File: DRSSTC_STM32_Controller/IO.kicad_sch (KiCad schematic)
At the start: 32 parts, among them J1 Conn_01x04, J10 Screw_Terminal_01x02, J11 Screw_Terminal_01x02, J12 Screw_Terminal_01x02, J6 Screw_Terminal_01x02, J7 Screw_Terminal_01x02, Q10 2N7002, Q5 2N7002, Q6 2N7002, Q7 2N7002, Q8 2N7002, Q9 2N7002

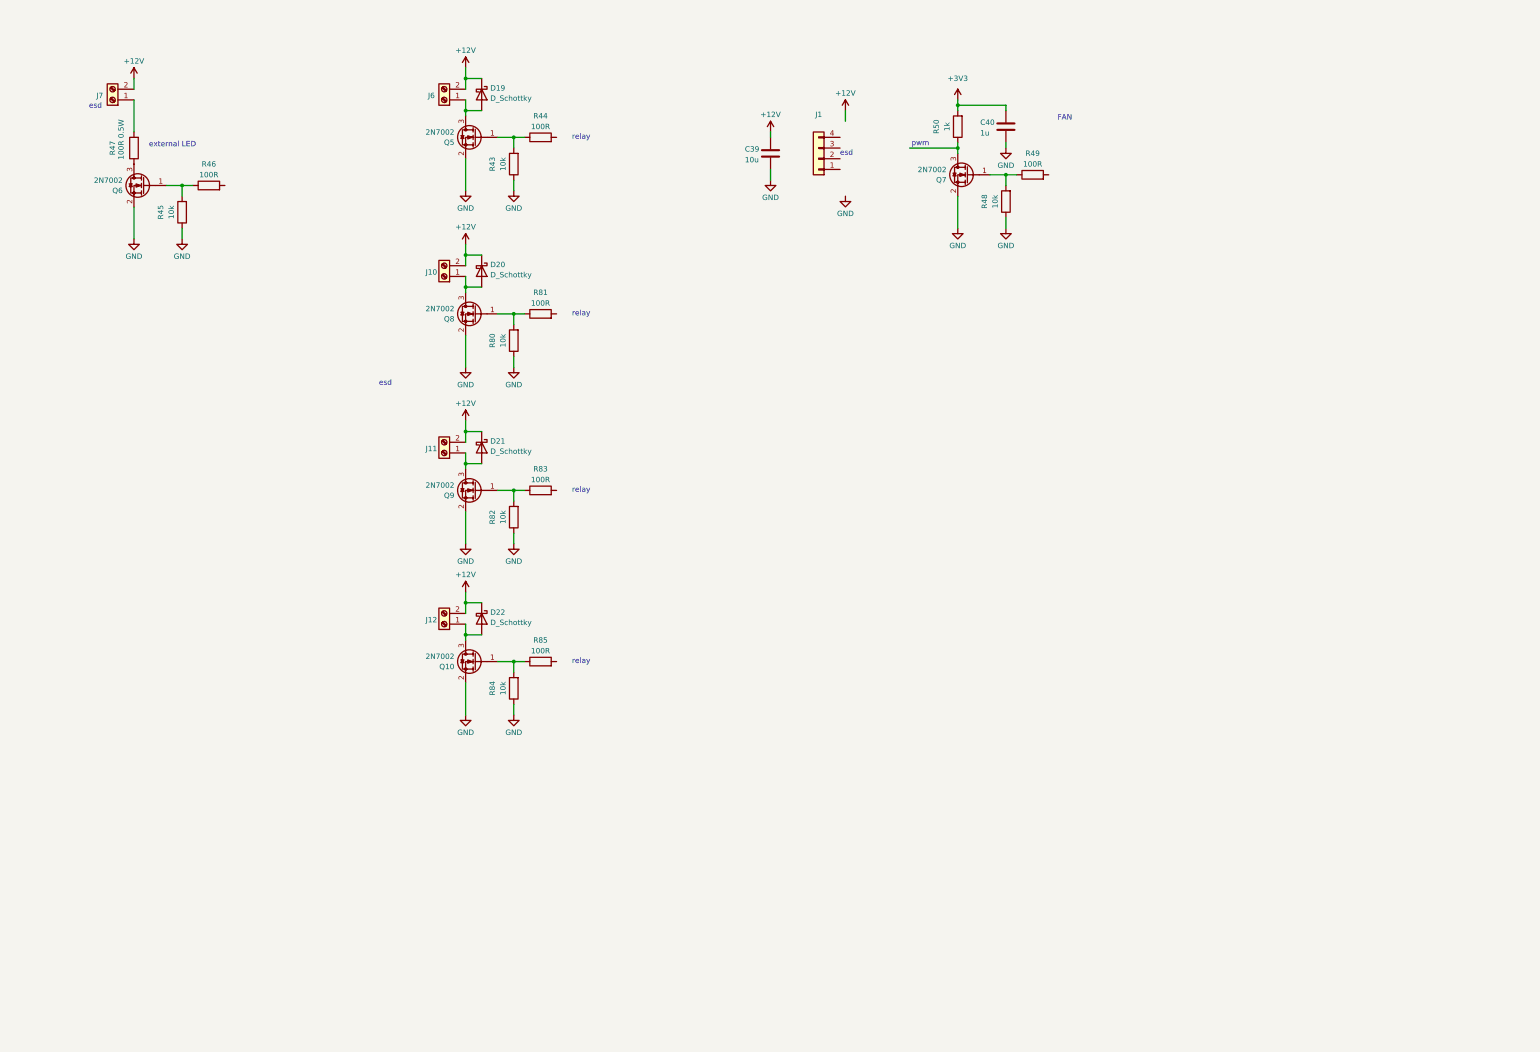
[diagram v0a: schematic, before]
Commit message: update the feedback stage simulation & controller schematic
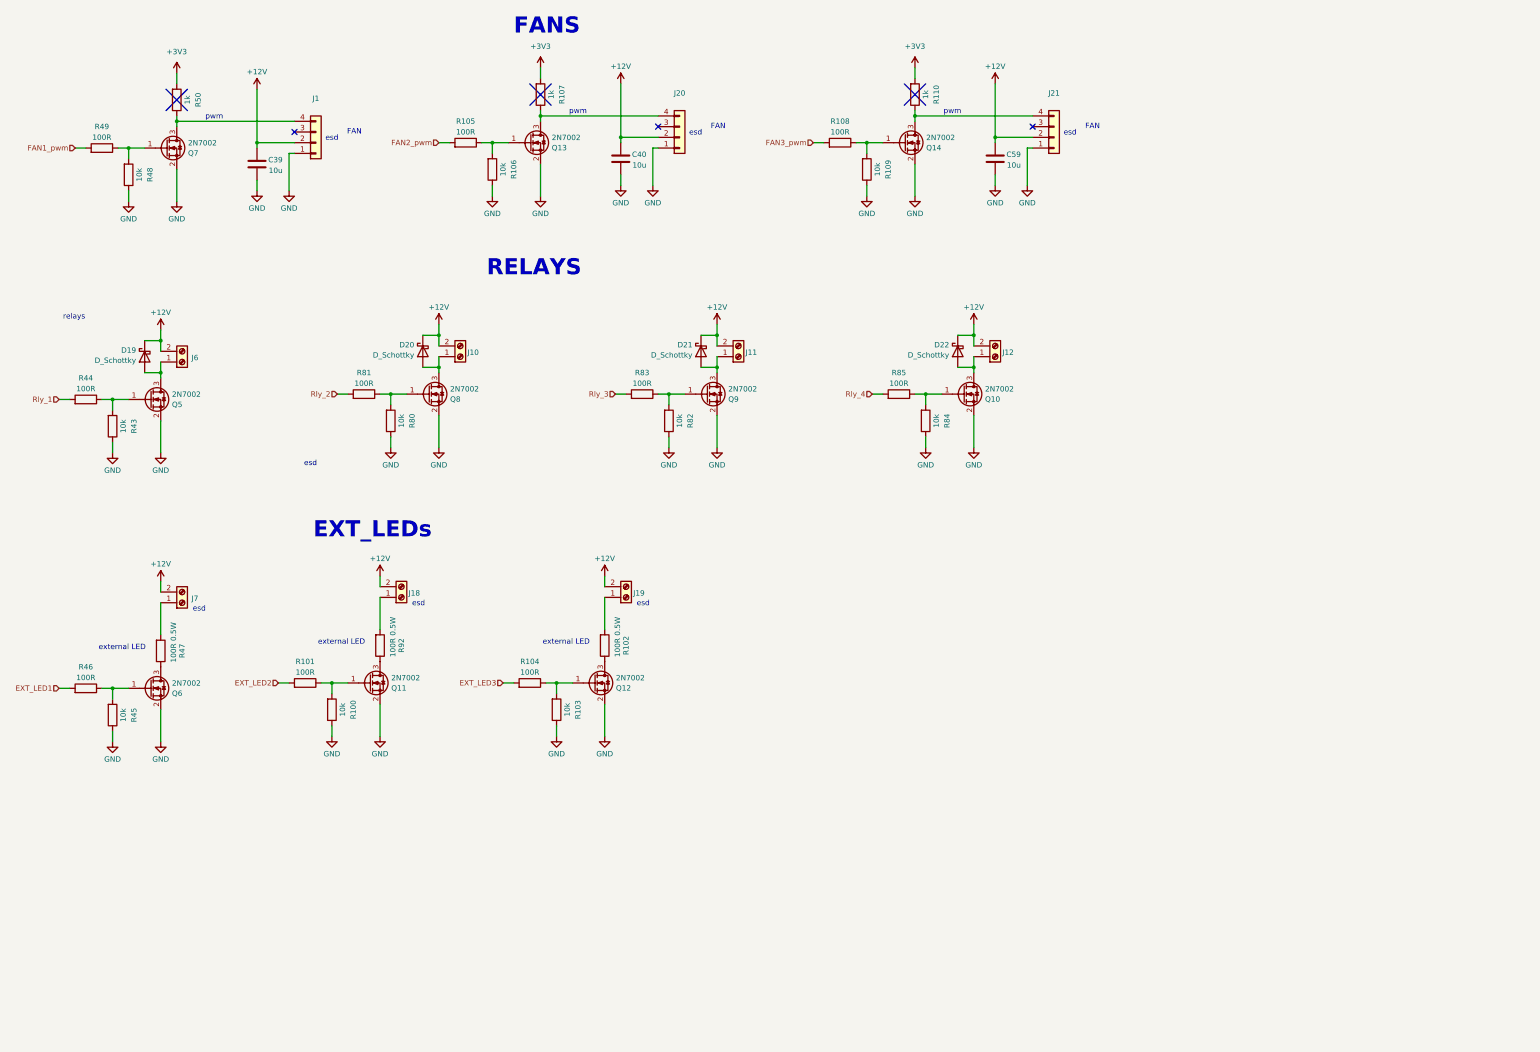
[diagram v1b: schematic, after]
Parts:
- added C59: 10u, Capacitor_SMD:C_0805_2012Metric, symbol Device:C
- added J18, J19: Screw_Terminal_01x02, TerminalBlock_Altech:Altech_AK100_1x02_P5.00mm, symbol Connector:Screw_Terminal_01x02
- added J20, J21: Conn_01x04, symbol Connector_Generic:Conn_01x04
- added Q11, Q12, Q13, Q14: 2N7002, Package_TO_SOT_SMD:SOT-23, symbol Transistor_FET:2N7002
- added R100, R103, R106, R109: 10k, Resistor_SMD:R_0805_2012Metric, symbol Device:R
- added R101, R104, R105, R108: 100R, Resistor_SMD:R_0805_2012Metric, symbol Device:R
- added R102, R92: 100R 0.5W, Resistor_SMD:R_0805_2012Metric, symbol Device:R
- added R107, R110: 1k, Resistor_SMD:R_0805_2012Metric, symbol Device:R
- C40: value 1u -> 10u
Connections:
- net +12V: now also C40.1, J1.2 (Pin_2), C59.1, J18.2 (Pin_2), J19.2 (Pin_2), J20.2 (Pin_2), J21.2 (Pin_2)
- net +3V3: now also R107.2, R110.2; no longer C40.1
- net GND: now also J1.1 (Pin_1), C59.2, J20.1 (Pin_1), J21.1 (Pin_1), Q11.2 (S), Q12.2 (S), Q13.2 (S), Q14.2 (S), R100.1, R103.1, R106.1, R109.1
- net Rly_3: now reaches R83.2
- net Rly_4: now reaches R85.2
- net FAN1_pwm: now reaches R49.2
- net Rly_2: now reaches R81.2
- net Rly_1: now reaches R44.2
- net EXT_LED1: now reaches R46.2
- net at Q7.3 (D), R50.1: now also J1.4 (Pin_4)
- new net: Q13.1 (G), R105.1, R106.2
- new net: Q14.1 (G), R108.1, R109.2
- new net: J21.4 (Pin_4), Q14.3 (D), R110.1
- new net: Q12.3 (D), R102.1
- new net: J19.1 (Pin_1), R102.2
- new net: Q11.1 (G), R100.2, R101.1
- new net: J18.1 (Pin_1), R92.2
- new net: Q12.1 (G), R103.2, R104.1
- new net: Q11.3 (D), R92.1
- new net: J20.4 (Pin_4), Q13.3 (D), R107.1
- new net EXT_LED2: R101.2
- new net EXT_LED3: R104.2
- new net FAN2_pwm: R105.2
- new net FAN3_pwm: R108.2
- no-connect marks 0 -> 3
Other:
- note added: "EXT_LEDs"
- note added: "FANS"
- note added: "RELAYS"
- note added: "relays"
- note removed: "relay"
- moved on the sheet: C39, D19, D20, D21, D22, J1, J10, J11, J12, J6, J7, Q10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

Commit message: update conroller schematics
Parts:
- removed J1, J20, J21: Conn_01x04, symbol Connector_Generic:Conn_01x04
- removed J10, J11, J12, J18, J19, J6, J7: Screw_Terminal_01x02, TerminalBlock_Altech:Altech_AK100_1x02_P5.00mm, symbol Connector:Screw_Terminal_01x02
- added C76: 10u, Capacitor_SMD:C_0805_2012Metric, symbol Device:C
- added Q19, Q20: 2N7002, Package_TO_SOT_SMD:SOT-23, symbol Transistor_FET:2N7002
- added R127, R130: 100R, Resistor_SMD:R_0805_2012Metric, symbol Device:R
- added R128, R131: 10k, Resistor_SMD:R_0805_2012Metric, symbol Device:R
- added R129: 1k, Resistor_SMD:R_0805_2012Metric, symbol Device:R
- added R132: 100R 0.5W, Resistor_SMD:R_0805_2012Metric, symbol Device:R
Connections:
- net +12V: now also C76.1
- net +3V3: now also R129.2
- net GND: now also C76.2, Q19.2 (S), Q20.2 (S), R128.1, R131.1
- net Relay4: now reaches D22.2 (A), Q10.3 (D)
- net FAN3cntrl: now reaches Q14.3 (D), R110.1
- net LED3: now reaches R102.2
- net Relay2: now reaches D20.2 (A), Q8.3 (D)
- net Relay3: now reaches D21.2 (A), Q9.3 (D)
- net LED1: now reaches R47.2
- net LED2: now reaches R92.2
- net FAN2cntrl: now reaches Q13.3 (D), R107.1
- net Relay1: now reaches D19.2 (A), Q5.3 (D)
- net FAN1cntrl: now reaches Q7.3 (D), R50.1
- new net: Q19.1 (G), R127.1, R128.2
- new net: Q20.1 (G), R130.1, R131.2
- new net: Q20.3 (D), R132.1
- new net EXT_LED4: R130.2
- new net FAN4_pwm: R127.2
- new net FAN4cntrl: Q19.3 (D), R129.1
- new net LED4: R132.2
- no-connect marks 3 -> 0
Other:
- note removed: "FAN"
- note removed: "relays"
- moved on the sheet: C39, C40, C59, D19, D20, D21, D22, Q10, Q11, Q12, Q13, Q14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

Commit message: assign footprints
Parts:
- D19, D20, D21, D22: footprint (none) -> Diode_SMD:D_SOD-128
- R100, R101, R103, R104, R105, R106, R107, R108, R109, R110, R127, R128, R129, R130, R131, R43, R44, R45, R46, R48, R49, R50, R80, R81, R82, R83, R84, R85: footprint Resistor_SMD:R_0805_2012Metric -> Resistor_SMD:R_0603_1608Metric
- R102, R132, R47, R92: footprint Resistor_SMD:R_0805_2012Metric -> Resistor_THT:R_Axial_DIN0309_L9.0mm_D3.2mm_P12.70mm_Horizontal
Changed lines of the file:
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@@
 			)
 		)
-		(property "Footprint" ""
+		(property "Footprint" "Diode_SMD:D_SOD-128"
 			(at 276.86 53.34 0)
 			(hide yes)
@@
 			)
 		)
-		(property "Footprint" "Resistor_SMD:R_0805_2012Metric"
+		(property "Footprint" "Resistor_SMD:R_0603_1608Metric"
 			(at 320.04 144.018 90)
 			(hide yes)
@@
 			)
 		)
-		(property "Footprint" "Resistor_SMD:R_0805_2012Metric"
+		(property "Footprint" "Resistor_SMD:R_0603_1608Metric"
 			(at 70.612 71.12 90)
 			(hide yes)
@@
 			)
 		)
-		(property "Footprint" "Resistor_SMD:R_0805_2012Metric"
+		(property "Footprint" "Resistor_SMD:R_0603_1608Metric"
 			(at 198.12 65.278 90)
 			(hide yes)
@@
 			)
 		)
-		(property "Footprint" "Resistor_SMD:R_0805_2012Metric"
+		(property "Footprint" "Resistor_SMD:R_0603_1608Metric"
 			(at 259.08 65.278 90)
 			(hide yes)
@@
 			)
 		)
-		(property "Footprint" "Resistor_SMD:R_0805_2012Metric"
+		(property "Footprint" "Resistor_SMD:R_0603_1608Metric"
 			(at 149.86 144.018 90)
 			(hide yes)
@@
 			)
 		)
-		(property "Footprint" "Resistor_SMD:R_0805_2012Metric"
+		(property "Footprint" "Resistor_SMD:R_0603_1608Metric"
 			(at 154.432 148.59 90)
 			(hide yes)
@@
 			)
 		)
-		(property "Footprint" "Resistor_SMD:R_0805_2012Metric"
+		(property "Footprint" "Resistor_SMD:R_0603_1608Metric"
 			(at 243.332 148.59 90)
 			(hide yes)
@@
 			)
 		)
-		(property "Footprint" "Resistor_SMD:R_0805_2012Metric"
+		(property "Footprint" "Resistor_THT:R_Axial_DIN0309_L9.0mm_D3.2mm_P12.70mm_Horizontal"
 			(at 184.912 229.87 90)
 			(hide yes)
@@
 			)
 		)
-		(property "Footprint" ""
+		(property "Footprint" "Diode_SMD:D_SOD-128"
 			(at 215.9 53.34 0)
 			(hide yes)
@@
 			)
 		)
-		(property "Footprint" "Resistor_SMD:R_0805_2012Metric"
+		(property "Footprint" "Resistor_SMD:R_0603_1608Metric"
 			(at 115.57 240.538 90)
 			(hide yes)
@@
 			)
 		)
-		(property "Footprint" "Resistor_SMD:R_0805_2012Metric"
+		(property "Footprint" "Resistor_SMD:R_0603_1608Metric"
 			(at 68.072 246.38 90)
 			(hide yes)
@@
 			)
 		)
-		(property "Footprint" "Resistor_SMD:R_0805_2012Metric"
+		(property "Footprint" "Resistor_SMD:R_0603_1608Metric"
 			(at 68.072 149.86 90)
 			(hide yes)
@@
 			)
 		)
-		(property "Footprint" "Resistor_SMD:R_0805_2012Metric"
+		(property "Footprint" "Resistor_SMD:R_0603_1608Metric"
 			(at 63.5 145.288 90)
 			(hide yes)
@@
 			)
 		)
-		(property "Footprint" "Resistor_SMD:R_0805_2012Metric"
+		(property "Footprint" "Resistor_SMD:R_0603_1608Metric"
 			(at 168.91 240.538 90)
 			(hide yes)
@@
 			)
 		)
-		(property "Footprint" ""
+		(property "Footprint" "Diode_SMD:D_SOD-128"
 			(at 149.86 53.34 0)
 			(hide yes)
@@
 			)
 		)
-		(property "Footprint" "Resistor_SMD:R_0805_2012Metric"
+		(property "Footprint" "Resistor_SMD:R_0603_1608Metric"
 			(at 132.08 65.278 90)
 			(hide yes)
@@
 			)
 		)
-		(property "Footprint" "Resistor_SMD:R_0805_2012Metric"
+		(property "Footprint" "Resistor_SMD:R_0603_1608Metric"
 			(at 324.612 148.59 90)
 			(hide yes)
@@
 			)
 		)
-		(property "Footprint" "Resistor_SMD:R_0805_2012Metric"
+		(property "Footprint" "Resistor_SMD:R_0603_1608Metric"
 			(at 66.04 66.548 90)
 			(hide yes)
@@
 			)
 		)
-		(property "Footprint" "Resistor_SMD:R_0805_2012Metric"
+		(property "Footprint" "Resistor_SMD:R_0603_1608Metric"
 			(at 254.762 130.81 90)
 			(hide yes)
@@
 			)
 		)
-		(property "Footprint" "Resistor_SMD:R_0805_2012Metric"
+		(property "Footprint" "Resistor_SMD:R_0603_1608Metric"
 			(at 238.76 144.018 90)
 			(hide yes)
@@
 			)
 		)
-		(property "Footprint" "Resistor_SMD:R_0805_2012Metric"
+		(property "Footprint" "Resistor_SMD:R_0603_1608Metric"
 			(at 120.142 245.11 90)
 			(hide yes)
@@
 			)
 		)
-		(property "Footprint" "Resistor_SMD:R_0805_2012Metric"
+		(property "Footprint" "Resistor_SMD:R_0603_1608Metric"
 			(at 63.5 241.808 90)
 			(hide yes)
@@
 			)
 		)
-		(property "Footprint" "Resistor_SMD:R_0805_2012Metric"
+		(property "Footprint" "Resistor_SMD:R_0603_1608Metric"
 			(at 136.652 69.85 90)
 			(hide yes)
@@
 			)
 		)
-		(property "Footprint" "Resistor_SMD:R_0805_2012Metric"
+		(property "Footprint" "Resistor_SMD:R_0603_1608Metric"
 			(at 173.482 245.11 90)
 			(hide yes)
@@
 			)
 		)
-		(property "Footprint" "Resistor_SMD:R_0805_2012Metric"
+		(property "Footprint" "Resistor_SMD:R_0603_1608Metric"
 			(at 79.502 132.08 90)
 			(hide yes)
@@
 			)
 		)
-		(property "Footprint" ""
+		(property "Footprint" "Diode_SMD:D_SOD-128"
 			(at 83.82 54.61 0)
 			(hide yes)
@@
 			)
 		)
-		(property "Footprint" "Resistor_SMD:R_0805_2012Metric"
+		(property "Footprint" "Resistor_SMD:R_0603_1608Metric"
 			(at 165.862 130.81 90)
 			(hide yes)
@@
 			)
 		)
-		(property "Footprint" "Resistor_SMD:R_0805_2012Metric"
+		(property "Footprint" "Resistor_SMD:R_0603_1608Metric"
 			(at 239.522 245.11 90)
 			(hide yes)
@@
 			)
 		)
-		(property "Footprint" "Resistor_SMD:R_0805_2012Metric"
+		(property "Footprint" "Resistor_SMD:R_0603_1608Metric"
 			(at 263.652 69.85 90)
 			(hide yes)
@@
 			)
 		)
-		(property "Footprint" "Resistor_SMD:R_0805_2012Metric"
+		(property "Footprint" "Resistor_THT:R_Axial_DIN0309_L9.0mm_D3.2mm_P12.70mm_Horizontal"
 			(at 79.502 231.14 90)
 			(hide yes)
@@
 			)
 		)
-		(property "Footprint" "Resistor_SMD:R_0805_2012Metric"
+		(property "Footprint" "Resistor_SMD:R_0603_1608Metric"
 			(at 202.692 69.85 90)
 			(hide yes)
@@
 			)
 		)
-		(property "Footprint" "Resistor_SMD:R_0805_2012Metric"
+		(property "Footprint" "Resistor_SMD:R_0603_1608Metric"
 			(at 234.95 240.538 90)
 			(hide yes)
@@
 			)
 		)
-		(property "Footprint" "Resistor_SMD:R_0805_2012Metric"
+		(property "Footprint" "Resistor_THT:R_Axial_DIN0309_L9.0mm_D3.2mm_P12.70mm_Horizontal"
 			(at 250.952 229.87 90)
 			(hide yes)
@@
 			)
 		)
-		(property "Footprint" "Resistor_SMD:R_0805_2012Metric"
+		(property "Footprint" "Resistor_SMD:R_0603_1608Metric"
 			(at 336.042 130.81 90)
 			(hide yes)
@@
 			)
 		)
-		(property "Footprint" "Resistor_SMD:R_0805_2012Metric"
+		(property "Footprint" "Resistor_THT:R_Axial_DIN0309_L9.0mm_D3.2mm_P12.70mm_Horizontal"
 			(at 131.572 229.87 90)
 			(hide yes)

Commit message: start cintrollenr routing
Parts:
- R102, R132, R47, R92: footprint Resistor_THT:R_Axial_DIN0309_L9.0mm_D3.2mm_P12.70mm_Horizontal -> Resistor_SMD:R_2512_6332Metric
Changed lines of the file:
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@@
 			)
 		)
-		(property "Footprint" "Resistor_THT:R_Axial_DIN0309_L9.0mm_D3.2mm_P12.70mm_Horizontal"
+		(property "Footprint" "Resistor_SMD:R_2512_6332Metric"
 			(at 184.912 229.87 90)
 			(hide yes)
@@
 			)
 		)
-		(property "Footprint" "Resistor_THT:R_Axial_DIN0309_L9.0mm_D3.2mm_P12.70mm_Horizontal"
+		(property "Footprint" "Resistor_SMD:R_2512_6332Metric"
 			(at 79.502 231.14 90)
 			(hide yes)
@@
 			)
 		)
-		(property "Footprint" "Resistor_THT:R_Axial_DIN0309_L9.0mm_D3.2mm_P12.70mm_Horizontal"
+		(property "Footprint" "Resistor_SMD:R_2512_6332Metric"
 			(at 250.952 229.87 90)
 			(hide yes)
@@
 			)
 		)
-		(property "Footprint" "Resistor_THT:R_Axial_DIN0309_L9.0mm_D3.2mm_P12.70mm_Horizontal"
+		(property "Footprint" "Resistor_SMD:R_2512_6332Metric"
 			(at 131.572 229.87 90)
 			(hide yes)
